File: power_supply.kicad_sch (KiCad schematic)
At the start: 18 parts, among them J1 USB_C_Receptacle_USB2.0_16P, J2 B2B-XH-A

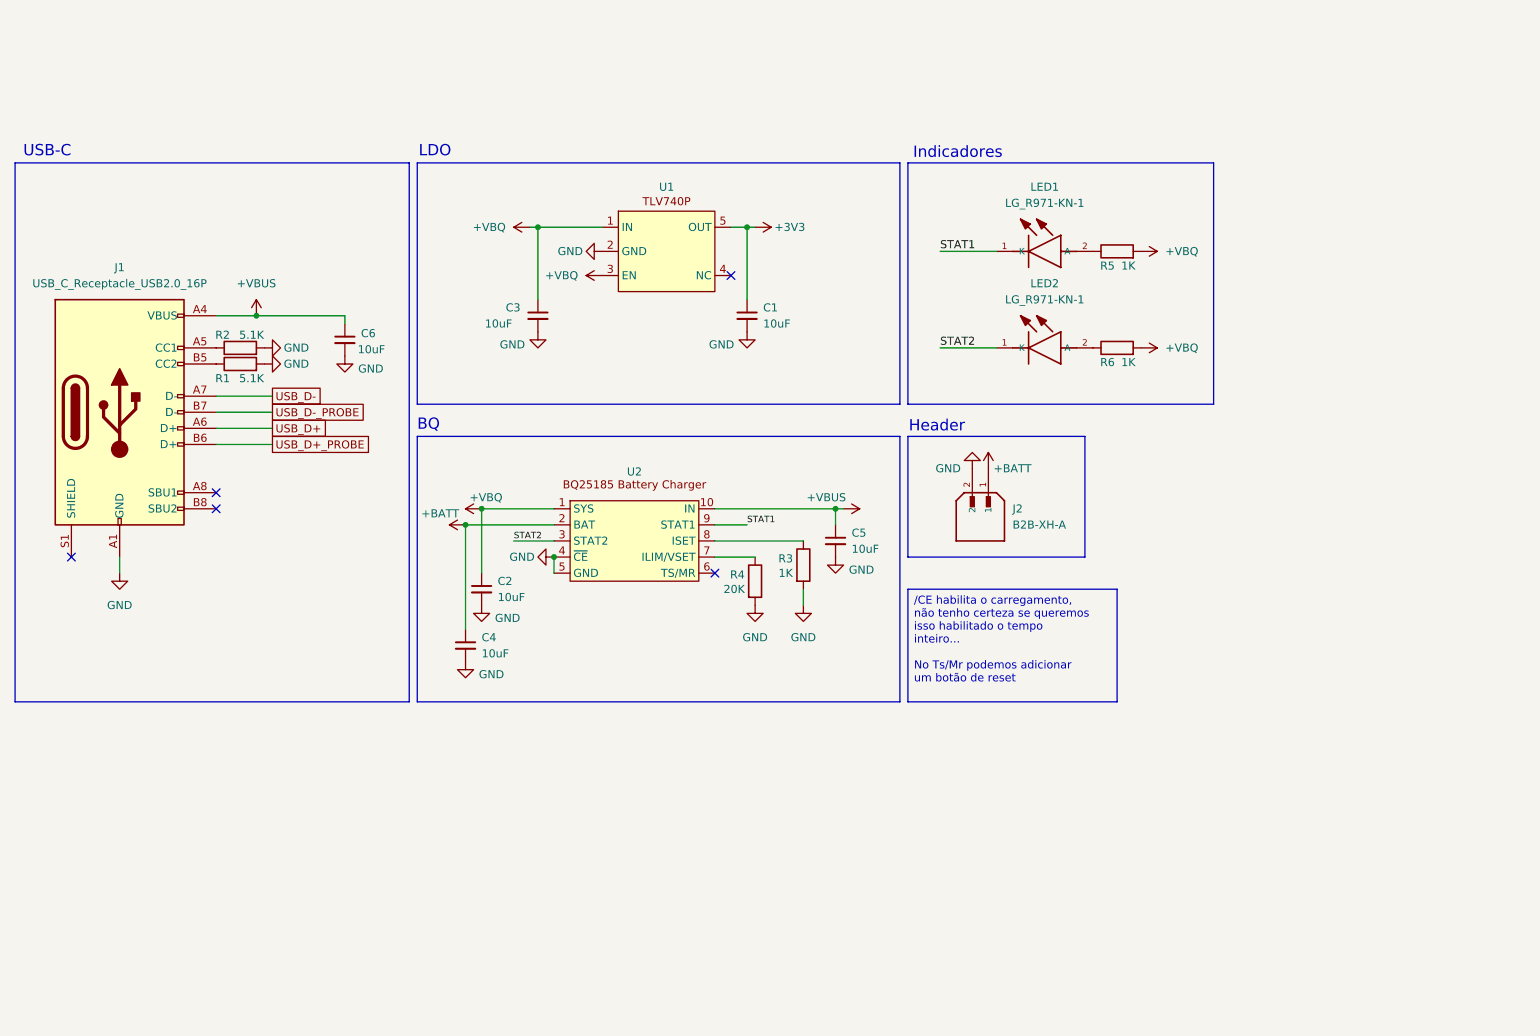
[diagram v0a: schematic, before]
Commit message: refac: changes resistor symbol to US pattern, adds second USB-C connector
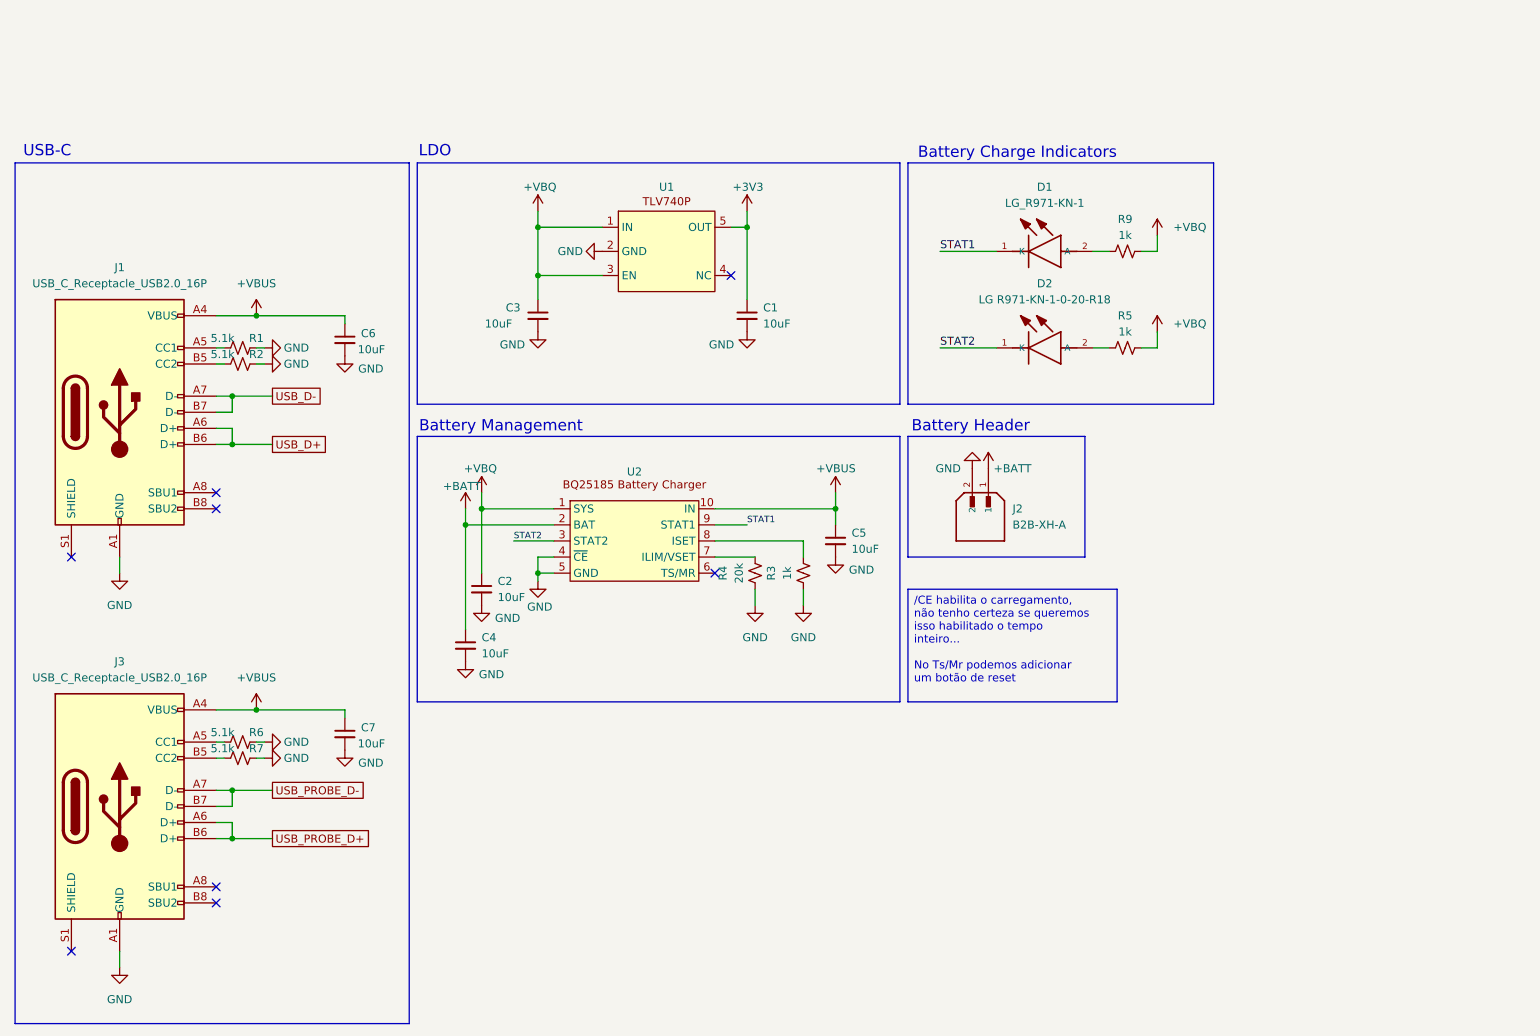
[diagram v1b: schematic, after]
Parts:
- removed R1, R2: 5.1K, symbol Device:R
- removed R3, R5, R6: 1K, symbol Device:R
- removed R4: 20K, symbol Device:R
- added C7: 10uF, symbol Device:C_Small
- added J3: USB_C_Receptacle_USB2.0_16P, symbol Connector:USB_C_Receptacle_USB2.0_16P
- added R1, R2, R6, R7: 5.1k, Resistor_SMD:R_0402_1005Metric, symbol Device:R_Small_US
- added R3, R5, R9: 1k, Resistor_SMD:R_0402_1005Metric, symbol Device:R_Small_US
- added R4: 20k, Resistor_SMD:R_0402_1005Metric, symbol Device:R_Small_US
- D1: renamed from LED1; MANUFACTURER_PART_NUMBER LG R971-KN-1 -> (none); MPN (none) -> LG R971-KN-1-0-20-R18
- D2: renamed from LED2; value LG_R971-KN-1 -> LG R971-KN-1-0-20-R18; MANUFACTURER_PART_NUMBER LG R971-KN-1 -> (none); MPN (none) -> LG R971-KN-1-0-20-R18
- J2: MP B2B-XH-A -> (none); MPN (none) -> B2B-XH-A
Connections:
- net USB_D+_PROBE is gone; now on net USB_D+: J1.B6 (D+)
- net USB_D-_PROBE is gone; now on net USB_D-: J1.B7 (D-)
- net +VBQ: now also R5.2, R9.2
- net +VBUS: now also C7.1, J3.A4 (VBUS), J3.A9 (VBUS), J3.B4 (VBUS), J3.B9 (VBUS)
- net GND: now also C7.2, J3.A1 (GND), J3.A12 (GND), J3.B1 (GND), J3.B12 (GND), R1.2, R2.2, R3.1, R4.1, R6.2, R7.2
- net at U2.7 (ILIM/VSET): now also R4.2
- net at U2.8 (ISET): now also R3.2
- net at J1.A5 (CC1): now also R1.1
- net at D1.2 (A): now also R9.1
- net at D2.2 (A): now also R5.1
- net at J1.B5 (CC2): now also R2.1
- new net: J3.A5 (CC1), R6.1
- new net: J3.B5 (CC2), R7.1
- new net USB_PROBE_D+: J3.A6 (D+), J3.B6 (D+)
- new net USB_PROBE_D-: J3.A7 (D-), J3.B7 (D-)
- no-connect marks 5 -> 8
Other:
- note added: "Battery Charge Indicators"
- note added: "Battery Header"
- note added: "Battery Management"
- note removed: "BQ"
- note removed: "Header"
- note removed: "Indicadores"

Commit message: refac: reannotates designators
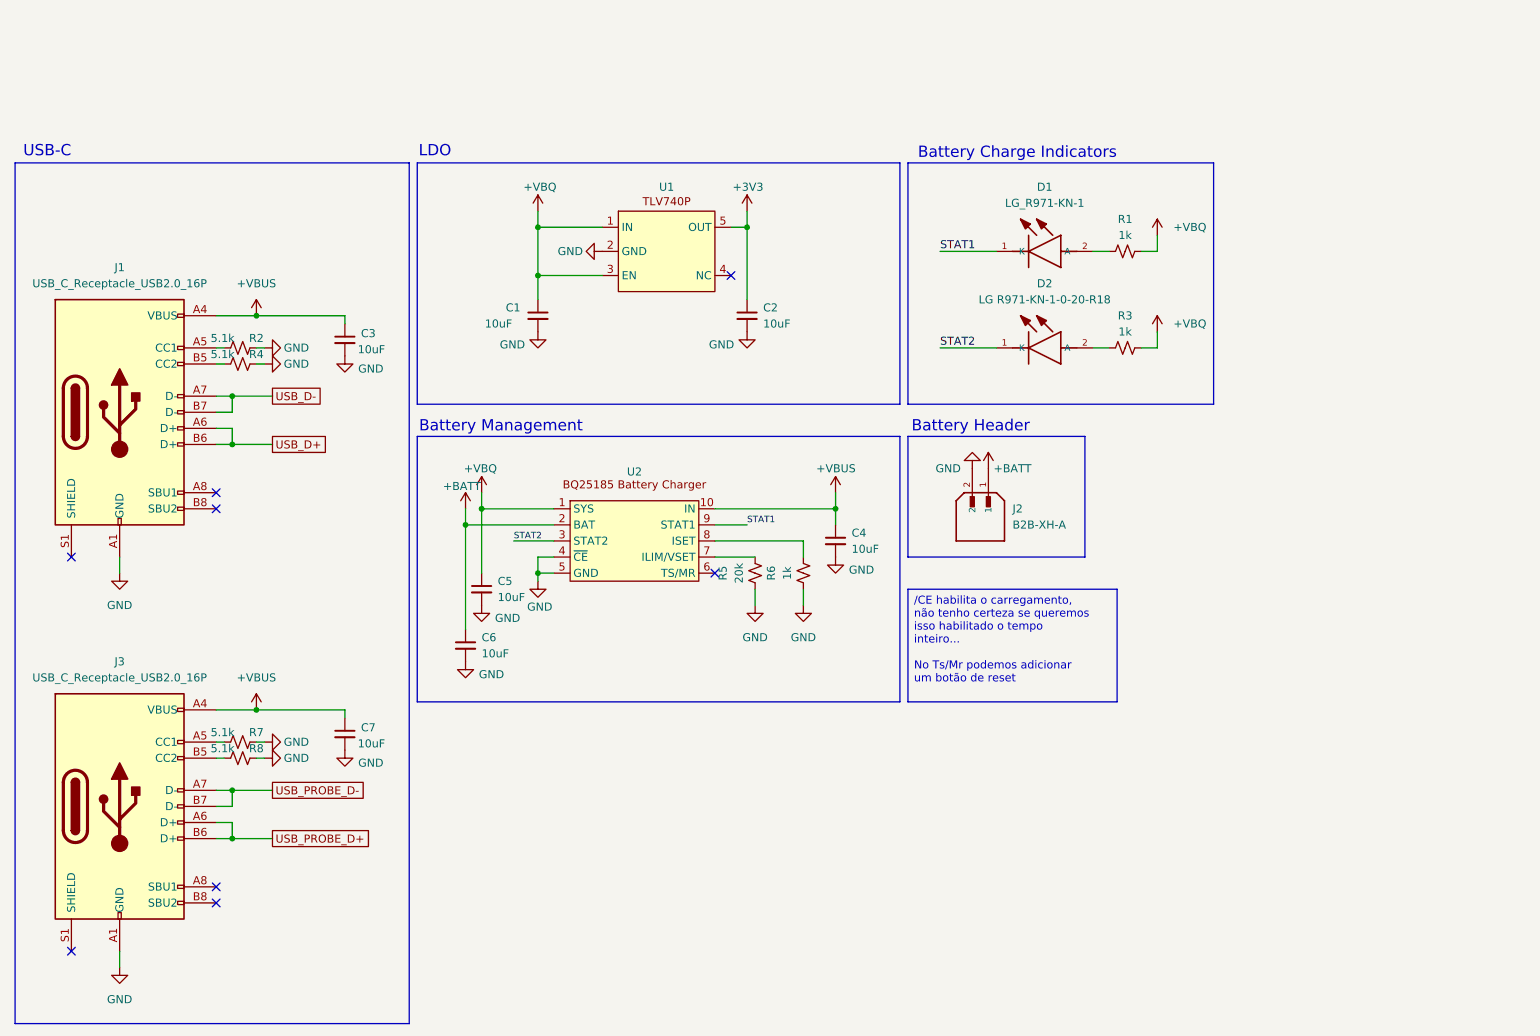
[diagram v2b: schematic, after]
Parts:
- renumbered C3 to C1, C1 to C2, C6 to C3, C5 to C4, C2 to C5, C4 to C6, R9 to R1, R1 to R2, R5 to R3, R2 to R4, R4 to R5, R3 to R6, R6 to R7, R7 to R8

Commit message: chore: adds titles to sheets and organizes root
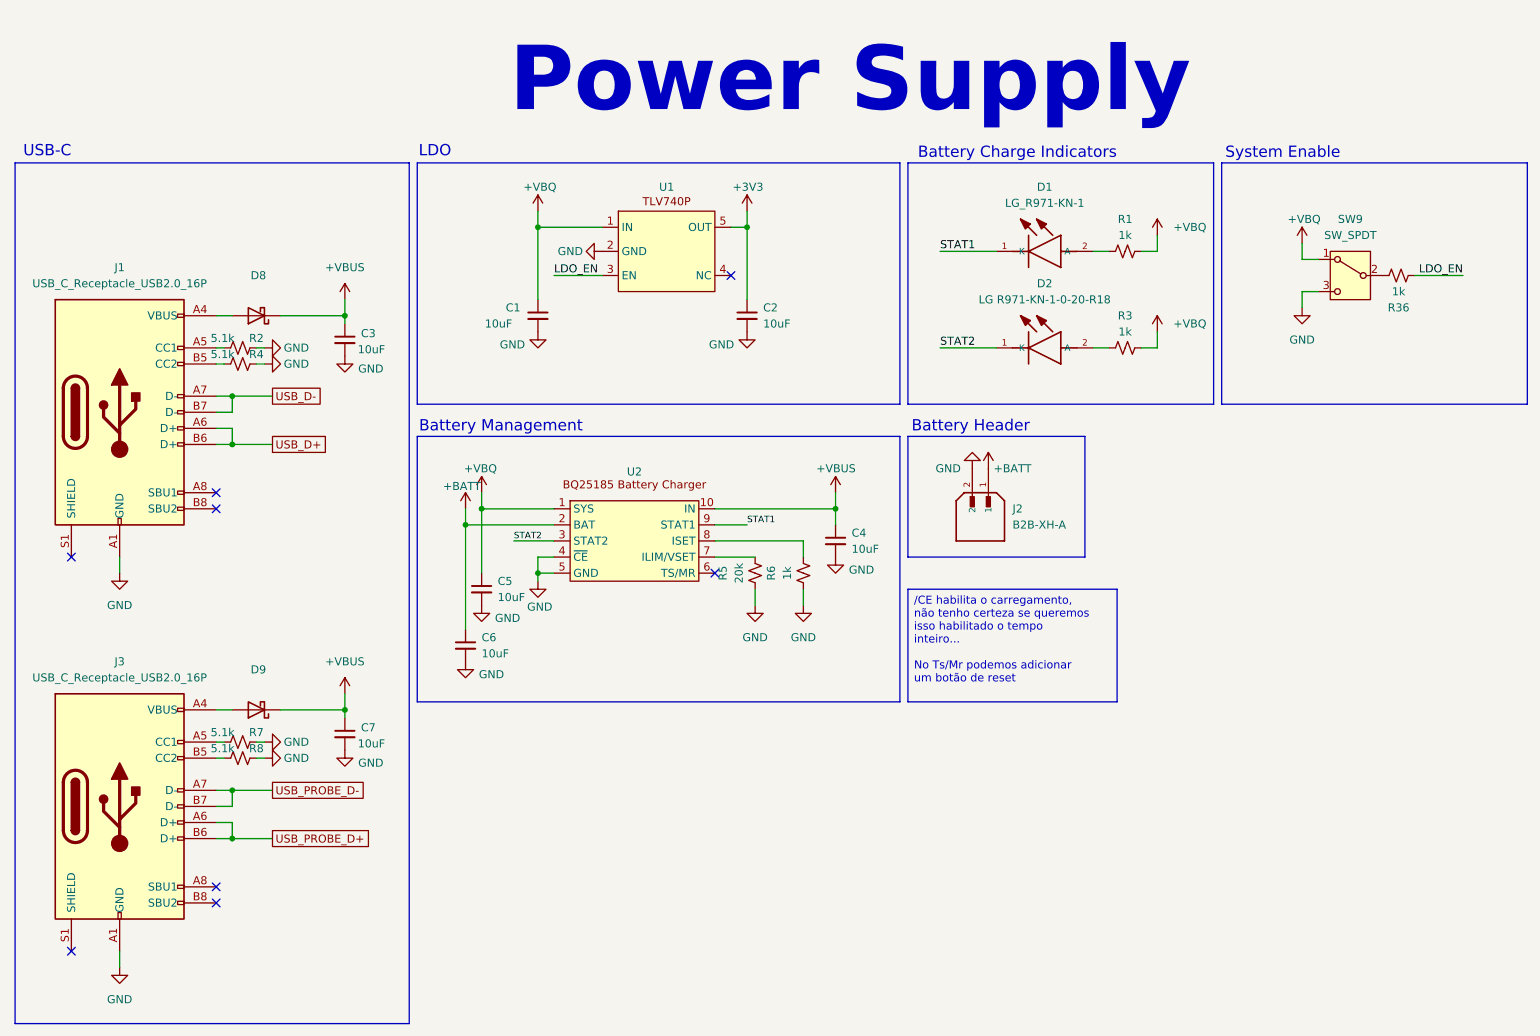
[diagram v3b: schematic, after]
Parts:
- added D8, D9: D_Schottky, symbol Device:D_Schottky
- added R36: 1k, Resistor_SMD:R_0402_1005Metric, symbol Device:R_Small_US
- added SW9: SW_SPDT, symbol Switch:SW_SPDT
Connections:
- net +VBQ: now also SW9.1 (A); no longer U1.3 (EN)
- net +VBUS: now also D8.1 (K), D9.1 (K); no longer J1.A4 (VBUS), J1.A9 (VBUS), J1.B4 (VBUS), J1.B9 (VBUS), J3.A4 (VBUS), J3.A9 (VBUS), J3.B4 (VBUS), J3.B9 (VBUS)
- net GND: now also SW9.3 (C)
- new net: D9.2 (A), J3.A4 (VBUS), J3.A9 (VBUS), J3.B4 (VBUS), J3.B9 (VBUS)
- new net: R36.2, SW9.2 (B)
- new net: D8.2 (A), J1.A4 (VBUS), J1.A9 (VBUS), J1.B4 (VBUS), J1.B9 (VBUS)
- new net LDO_EN: R36.1, U1.3 (EN)
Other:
- note added: "Power Supply"
- note added: "System Enable"

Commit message: refac: standardizes schematic sectorization
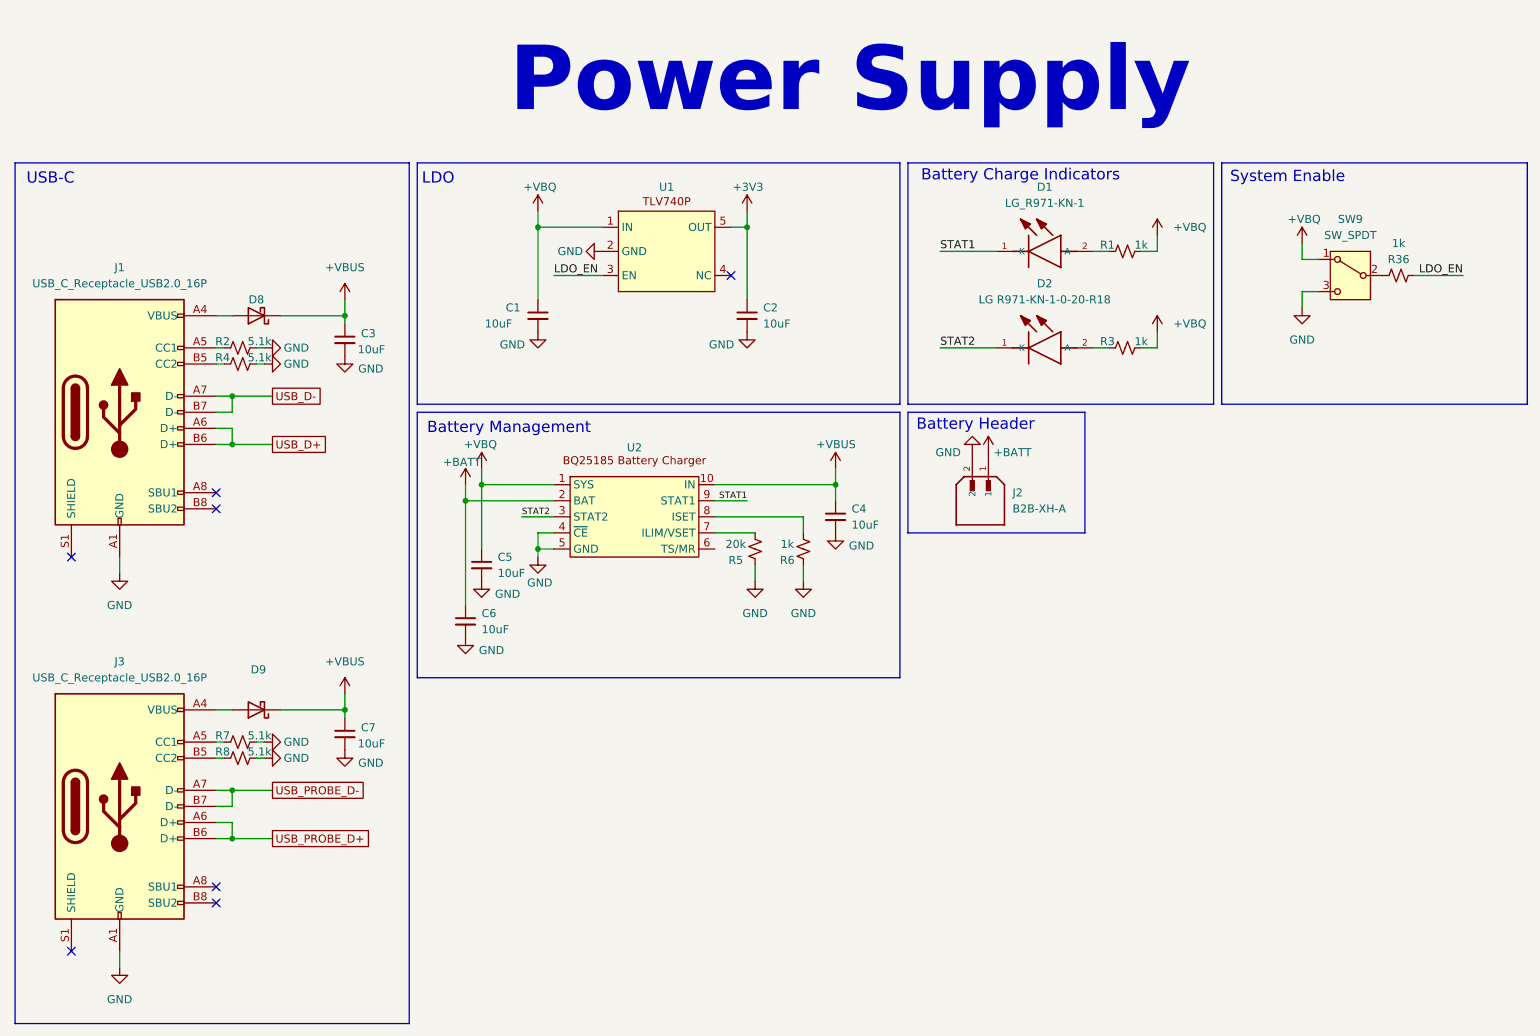
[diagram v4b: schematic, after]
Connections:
- no-connect marks 8 -> 7
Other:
- moved on the sheet: C4, C5, C6, J2, R5, R6, U2

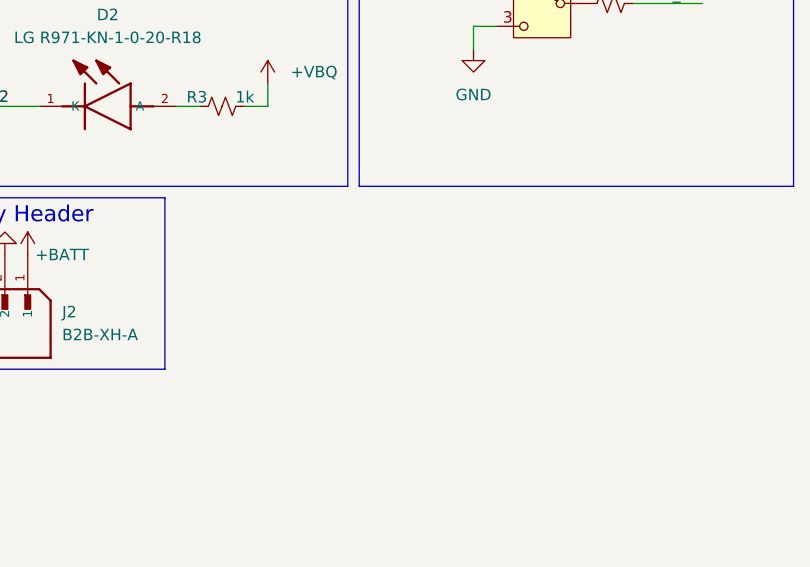
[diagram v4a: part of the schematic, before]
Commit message: feat: adds 0R for BQ bypass
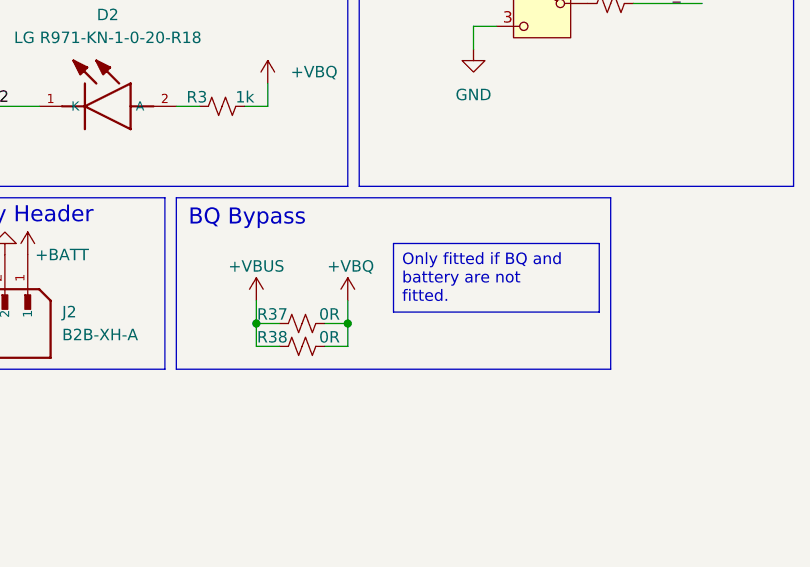
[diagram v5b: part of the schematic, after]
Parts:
- added R37, R38: 0R, Resistor_SMD:R_1206_3216Metric, symbol Device:R_Small_US
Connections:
- net +VBQ: now also R37.2, R38.2
- net +VBUS: now also R37.1, R38.1
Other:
- note added: "BQ Bypass"

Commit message: refac: unfits battery circuitry
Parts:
- removed C6, C7: 10uF, symbol Device:C_Small
- added R39: 10k, Resistor_SMD:R_0402_1005Metric, symbol Device:R_Small_US
- C1, C2: value 10uF -> 10u; footprint (none) -> Capacitor_SMD:C_0805_2012Metric; MPN (none) -> CL21A106KOQNNNG
- C3, C4, C5: value 10uF -> 10u; footprint (none) -> Capacitor_SMD:C_0805_2012Metric; MPN (none) -> CL21A106KOQNNNG; now not fitted
- J2, R5, R6, U2: now not fitted
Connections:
- net +BATT: now also C3.1
- net +VBUS: no longer C3.1
- net GND: now also R39.1
- net at U2.6 (TS/MR): now also R39.2
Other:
- moved on the sheet: C1, R36
